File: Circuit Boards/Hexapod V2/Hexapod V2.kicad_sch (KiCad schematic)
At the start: 23 parts, among them U1 MPU6050, U2 NRF24L01_Breakout

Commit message: added new stuff
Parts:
- added BZ1: Buzzer, symbol Device:Buzzer
- added C2: 0.1μF, Capacitor_THT:CP_Radial_D4.0mm_P1.50mm, symbol Device:C
- added C3, C4: 100μF, Capacitor_THT:CP_Radial_D5.0mm_P2.50mm, symbol Device:C
- added C5: 11μF, Capacitor_THT:CP_Radial_D4.0mm_P1.50mm, symbol Device:C
- added D2: WS2812B, LED_SMD:LED_WS2812B_PLCC4_5.0x5.0mm_P3.2mm, symbol LED:WS2812B
- added D3: D, Diode_THT:D_5KP_P12.70mm_Horizontal, symbol Device:D
- added J1: Battery, TerminalBlock_Phoenix:TerminalBlock_Phoenix_MKDS-1,5-2-5.08_1x02_P5.08mm_Horizontal, symbol Connector:Screw_Terminal_01x02
- added J2: Conn_01x14_Pin, Connector_PinSocket_2.54mm:PinSocket_1x14_P2.54mm_Vertical, symbol Connector:Conn_01x14_Pin
- added R1: 10kΩ, Resistor_THT:R_Axial_DIN0207_L6.3mm_D2.5mm_P7.62mm_Horizontal, symbol Device:R
- added R2: 20kΩ, Resistor_THT:R_Axial_DIN0207_L6.3mm_D2.5mm_P7.62mm_Horizontal, symbol Device:R
- added U3: Buck Converter, usini_sensors:YAAJ_DCDC_StepDown_LM2596, symbol Nice Modules:YAAJ_DCDC_StepDown_LM2596
- A1: footprint PCM_arduino-library:Clone_Mega2560_Pro_Socket -> Arduino Library:Clone_Mega2560_Pro_Socket
- C1: value C -> 0.1μF; footprint (none) -> Capacitor_THT:CP_Radial_D4.0mm_P1.50mm
- renumbered Servo11 to Servo10, Servo14 to Servo11, Servo17 to Servo12, Servo3 to Servo13, Servo6 to Servo14, Servo9 to Servo15, Servo12 to Servo16, Servo15 to Servo17, Servo4 to Servo2, Servo7 to Servo3, Servo10 to Servo4, Servo13 to Servo5, Servo16 to Servo6, Servo2 to Servo7, Servo5 to Servo8, Servo8 to Servo9
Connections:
- net +3.3V: no longer U2.2 (VCC)
- net +5V: now also C2.1, D2.1 (VDD), J2.1 (Pin_1); no longer Servo1.2 (Pin_2), Servo10.2 (Pin_2), Servo11.2 (Pin_2), Servo12.2 (Pin_2), Servo13.2 (Pin_2), Servo14.2 (Pin_2), Servo15.2 (Pin_2), Servo16.2 (Pin_2), Servo17.2 (Pin_2), Servo18.2 (Pin_2), Servo2.2 (Pin_2), Servo3.2 (Pin_2), Servo4.2 (Pin_2), Servo5.2 (Pin_2), Servo6.2 (Pin_2), Servo7.2 (Pin_2), Servo8.2 (Pin_2), Servo9.2 (Pin_2)
- net CSN: now also A1.D53 (D53_CS)
- net GND: now also D1.3 (VSS), BZ1.2 (-), C2.2, C3.2, C4.2, C5.2, D2.3 (VSS), D3.2 (A), J2.2 (Pin_2), R1.2, U3.1 (Vin)
- net MISO: now also A1.D50 (D50_MISO), J2.12 (Pin_12), J2.6 (Pin_6)
- net MOSI: now also A1.D51 (D51_MOSI), J2.13 (Pin_13), J2.9 (Pin_9)
- net S1: now also A1.D7; no longer A1.D22
- net S10: now also A1.D33; no longer A1.D31
- net S11: now also A1.D35; no longer A1.D32
- net S12: now also A1.D37; no longer A1.D33
- net S13: now also A1.D39; no longer A1.D34
- net S14: now also A1.D41; no longer A1.D35
- net S15: now also A1.D43; no longer A1.D36
- net S16: now also A1.D45; no longer A1.D37
- net S17: now also A1.D47; no longer A1.D38
- net S18: now also A1.D49; no longer A1.D39
- net S2: now also A1.D9; no longer A1.D23
- net S3: now also A1.D11; no longer A1.D24
- net S4: now also A1.D13; no longer A1.D25
- net S5: now also A1.D23; no longer A1.D26
- net S6: now also A1.D25; no longer A1.D27
- net S7: now also A1.D27; no longer A1.D28
- net S9: now also A1.D31; no longer A1.D30
- net SCK: now also A1.D52 (D52_SCK), J2.10 (Pin_10), J2.7 (Pin_7)
- net VIN: now also A1.VIN2 (VIN), Servo1.2 (Pin_2), Servo10.2 (Pin_2), Servo11.2 (Pin_2), Servo12.2 (Pin_2), Servo13.2 (Pin_2), Servo14.2 (Pin_2), Servo15.2 (Pin_2), Servo16.2 (Pin_2), Servo17.2 (Pin_2), Servo18.2 (Pin_2), Servo2.2 (Pin_2), Servo3.2 (Pin_2), Servo4.2 (Pin_2), Servo5.2 (Pin_2), Servo6.2 (Pin_2), Servo7.2 (Pin_2), Servo8.2 (Pin_2), Servo9.2 (Pin_2), C3.1, C4.1, D3.1 (K), R2.2, U3.2 (GND)
- net A0: now reaches A1.A0
- net A2: now reaches A1.A2
- net A2: now also BZ1.1 (+)
- new net: C5.1, U2.2 (VCC)
- new net: J1.2 (Pin_2), U3.3 (GND)
- new net A1: R1.1, R2.1
- new net CS - Display: J2.3 (Pin_3)
- new net CS - Touch: J2.11 (Pin_11)
- new net DC/RC: J2.5 (Pin_5)
- new net LED: J2.8 (Pin_8)
- new net LED2: D2.4 (DIN)
- no-connect marks 6 -> 9
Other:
- title: (none) -> Hexapod PCB V2
- moved on the sheet: A1, Servo1, Servo10, Servo11, Servo12, Servo13, Servo14, Servo15, Servo16, Servo17, Servo18, Servo2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

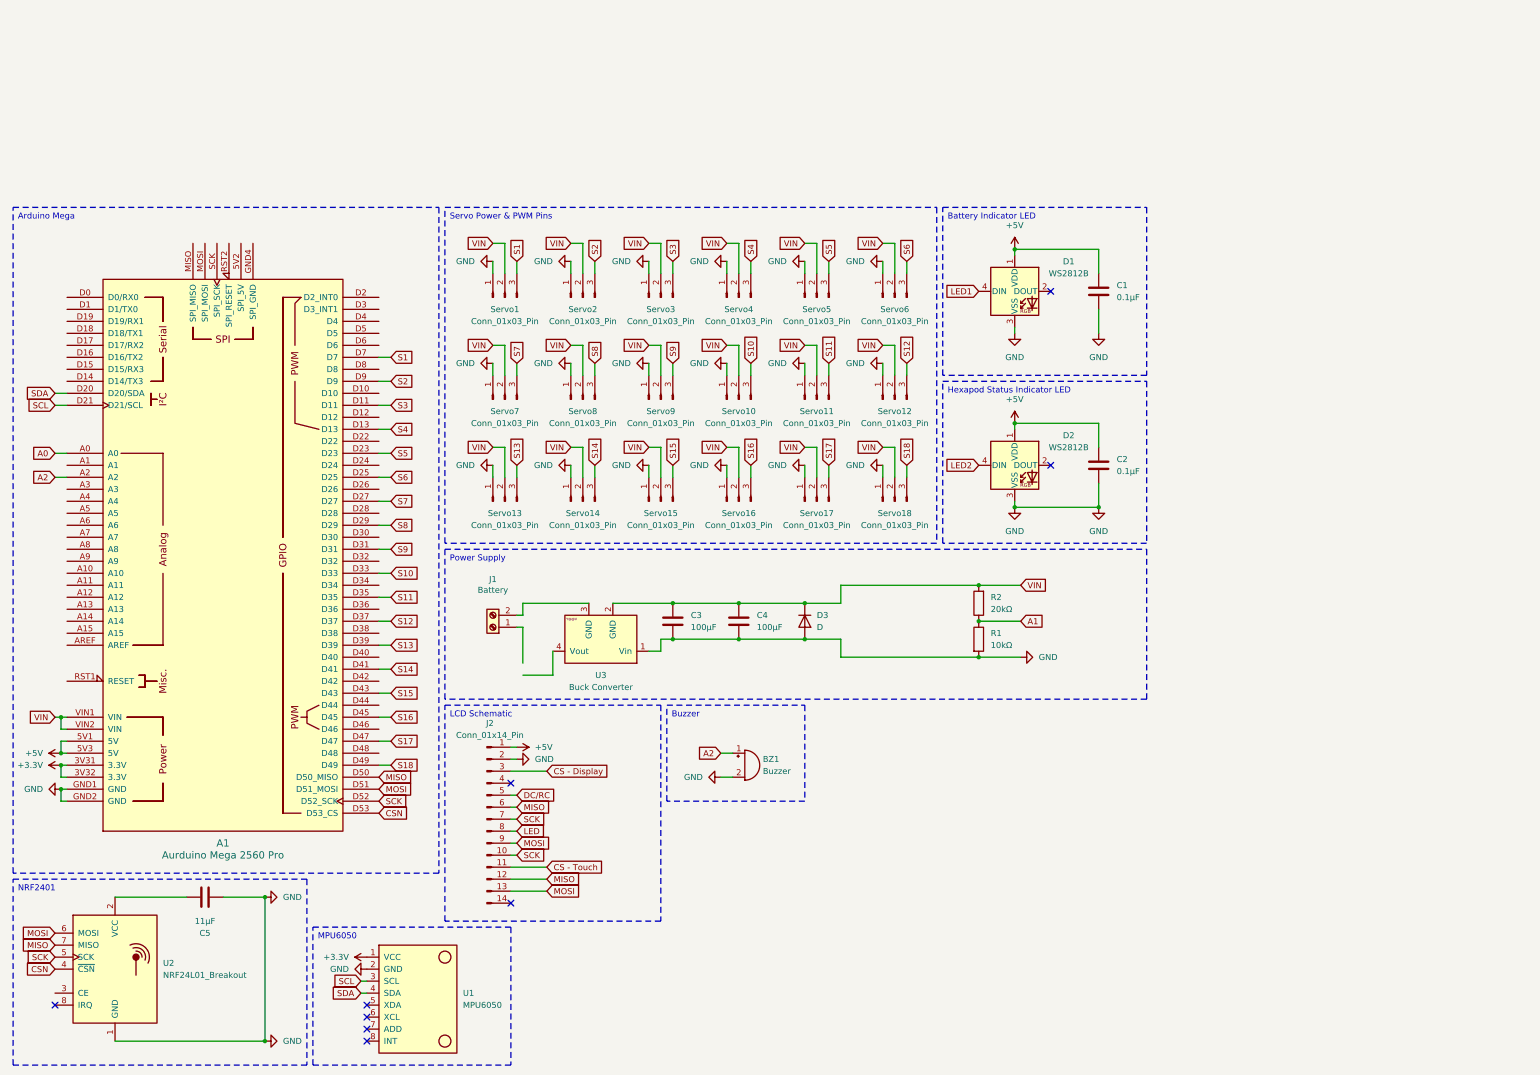
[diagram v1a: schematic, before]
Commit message: Started Firmware + Continued PCB
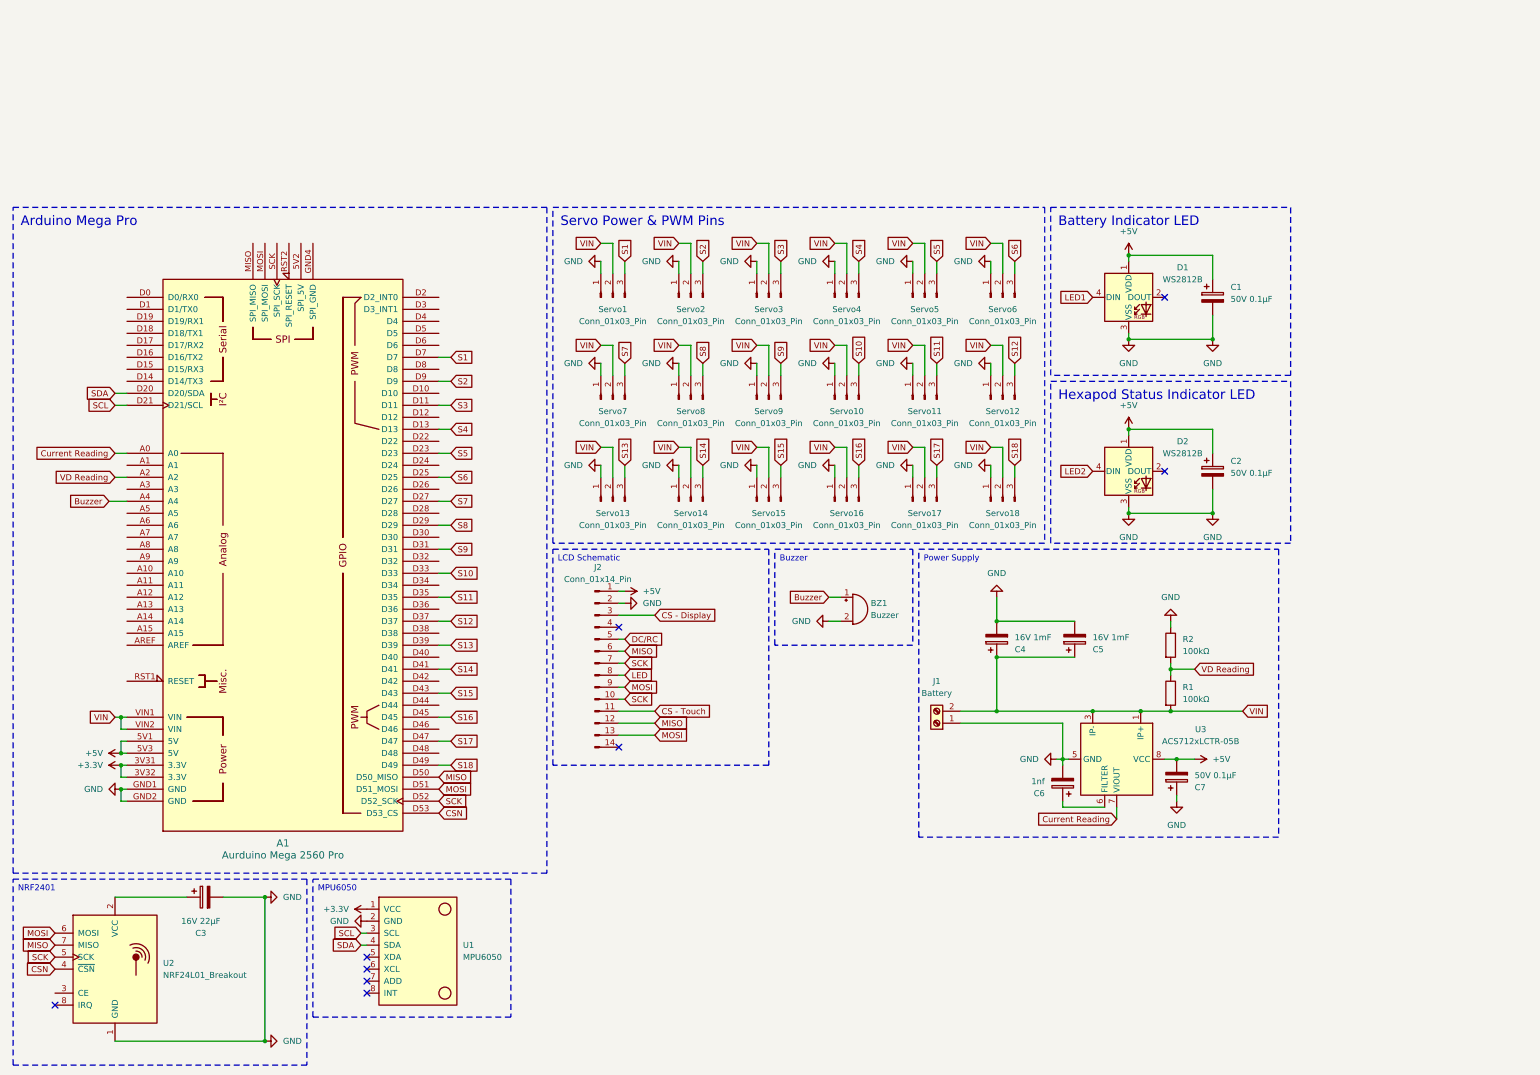
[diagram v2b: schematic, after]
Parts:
- removed C1, C2: 0.1μF, Capacitor_THT:CP_Radial_D4.0mm_P1.50mm, symbol Device:C
- removed C3, C4: 100μF, Capacitor_THT:CP_Radial_D5.0mm_P2.50mm, symbol Device:C
- removed C5: 11μF, Capacitor_THT:CP_Radial_D4.0mm_P1.50mm, symbol Device:C
- removed D3: D, Diode_THT:D_5KP_P12.70mm_Horizontal, symbol Device:D
- removed U3: Buck Converter, usini_sensors:YAAJ_DCDC_StepDown_LM2596, symbol Nice Modules:YAAJ_DCDC_StepDown_LM2596
- added C1, C2, C7: 50V 0.1μF, symbol Device:C_Polarized
- added C3: 16V 22μF, symbol Device:C_Polarized
- added C4, C5: 16V 1mF, symbol Device:C_Polarized
- added C6: 1nf, symbol Device:C_Polarized
- added U3: ACS712xLCTR-05B, Package_SO:SOIC-8_3.9x4.9mm_P1.27mm, symbol Sensor_Current:ACS712xLCTR-05B
- BZ1: footprint (none) -> Buzzer_Beeper:Buzzer_12x9.5RM7.6
- J1: footprint TerminalBlock_Phoenix:TerminalBlock_Phoenix_MKDS-1,5-2-5.08_1x02_P5.08mm_Horizontal -> (none)
- R1: value 10kΩ -> 100kΩ; footprint Resistor_THT:R_Axial_DIN0207_L6.3mm_D2.5mm_P7.62mm_Horizontal -> (none)
- R2: value 20kΩ -> 100kΩ; footprint Resistor_THT:R_Axial_DIN0207_L6.3mm_D2.5mm_P7.62mm_Horizontal -> (none)
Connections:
- net +5V: now also C1.1, C2.1, C7.2, U3.8 (VCC)
- net GND: now also J1.1 (Pin_1), R2.1, C1.2, C2.2, C3.2, C4.2, C5.2, C6.2, C7.1, U3.5 (GND); no longer R1.2
- net VIN: now also J1.2 (Pin_2), R1.2, C4.1, C5.1, U3.1 (IP+), U3.2 (IP+), U3.3 (IP-), U3.4 (IP-); no longer R2.2
- net at U2.2 (VCC): now also C3.1
- net Buzzer: now reaches A1.A4
- net Buzzer: now also BZ1.1 (+)
- net A0 renamed Current Reading 
- net A1 renamed VD Reading
- net VD Reading: now also A1.A2, R2.2; no longer R2.1
- removed net A2: A1.A2, BZ1.1 (+)
- new net: C6.1, U3.6 (FILTER)
- new net Current Reading: U3.7 (VIOUT)
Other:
- moved on the sheet: A1, BZ1, D1, D2, J2, Servo1, Servo10, Servo11, Servo12, Servo13, Servo14, Servo15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
